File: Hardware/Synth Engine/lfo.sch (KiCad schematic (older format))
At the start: 26 parts, among them J12 Conn_01x08, J5 Conn_01x02, J6 Conn_01x03, U4 TL074, U5 TL074

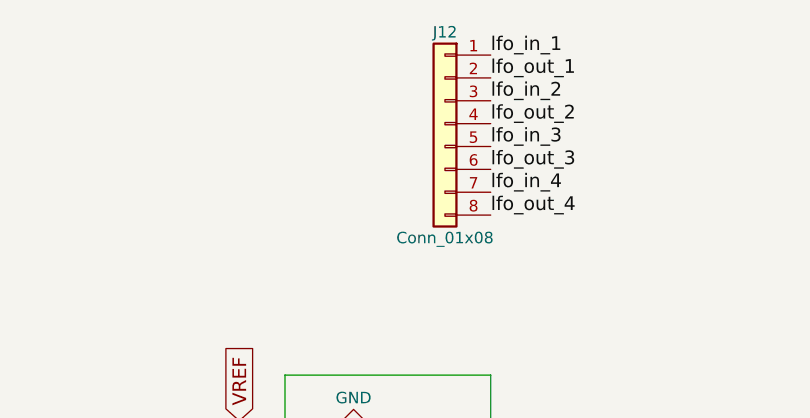
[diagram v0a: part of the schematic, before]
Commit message: fix LFO connector schem
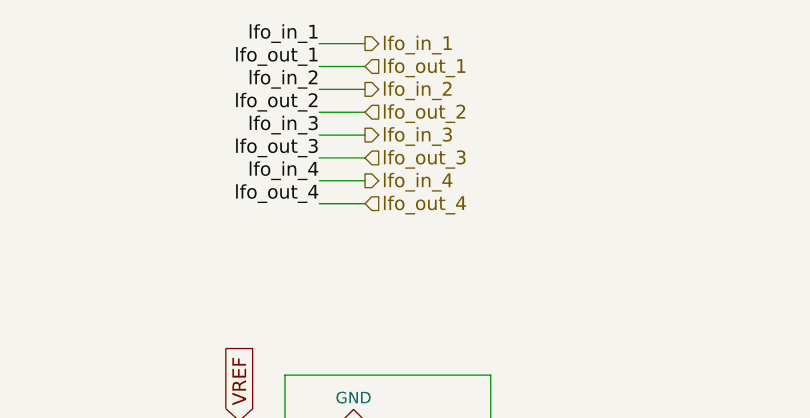
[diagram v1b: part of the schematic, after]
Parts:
- removed J12: Conn_01x08, Pin_Headers:Pin_Header_Straight_1x08_Pitch2.54mm, symbol Conn_01x08
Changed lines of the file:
@@
 Text Label 10000 5250 0    60   ~ 0
 lfo_out_4
-Text Label 6350 800  0    60   ~ 0
+Text Label 5600 750  2    60   ~ 0
 lfo_in_1
-Text Label 6350 900  0    60   ~ 0
+Text Label 5600 850  2    60   ~ 0
 lfo_out_1
-Text Label 6350 1000 0    60   ~ 0
+Text Label 5600 950  2    60   ~ 0
 lfo_in_2
-Text Label 6350 1100 0    60   ~ 0
+Text Label 5600 1050 2    60   ~ 0
 lfo_out_2
-Text Label 6350 1200 0    60   ~ 0
+Text Label 5600 1150 2    60   ~ 0
 lfo_in_3
-Text Label 6350 1300 0    60   ~ 0
+Text Label 5600 1250 2    60   ~ 0
 lfo_out_3
-Text Label 6350 1400 0    60   ~ 0
+Text Label 5600 1350 2    60   ~ 0
 lfo_in_4
-Text Label 6350 1500 0    60   ~ 0
+Text Label 5600 1450 2    60   ~ 0
 lfo_out_4
-$Comp
-L Conn_01x08 J12
-U 1 1 5C638F36
-P 6150 1100
-F 0 "J12" H 6150 1500 50  0000 C CNN
-F 1 "Conn_01x08" H 6150 600 50  0000 C CNN
-F 2 "Pin_Headers:Pin_Header_Straight_1x08_Pitch2.54mm" H 6150 1100 50  0001 C CNN
-F 3 "" H 6150 1100 50  0001 C CNN
-	1    6150 1100
-	-1   0    0    -1
-$EndComp
+Text HLabel 5800 750  2    60   Output ~ 0
+lfo_in_1
+Text HLabel 5800 850  2    60   Input ~ 0
+lfo_out_1
+Text HLabel 5800 950  2    60   Output ~ 0
+lfo_in_2
+Text HLabel 5800 1050 2    60   Input ~ 0
+lfo_out_2
+Text HLabel 5800 1150 2    60   Output ~ 0
+lfo_in_3
+Text HLabel 5800 1250 2    60   Input ~ 0
+lfo_out_3
+Text HLabel 5800 1350 2    60   Output ~ 0
+lfo_in_4
+Text HLabel 5800 1450 2    60   Input ~ 0
+lfo_out_4
+Wire Wire Line
+	5600 750  5800 750
+Wire Wire Line
+	5600 850  5800 850
+Wire Wire Line
+	5800 950  5600 950
+Wire Wire Line
+	5600 1050 5800 1050
+Wire Wire Line
+	5800 1150 5600 1150
+Wire Wire Line
+	5600 1250 5800 1250
+Wire Wire Line
+	5800 1350 5600 1350
+Wire Wire Line
+	5600 1450 5800 1450
 $EndSCHEMATC

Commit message: route LFO
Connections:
- net main_lfo: now also U5.10 (+), U5.12 (+), U5.5 (+); no longer U5.10 (+), U5.12 (+), U5.5 (+)
- new net: C76.1, U5.13 (-), U5.14
- new net: C74.1, U5.8, U5.9 (-)
- new net: C77.1, U5.6 (-), U5.7
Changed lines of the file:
@@
 $Comp
 L TL074 U5
-U 2 1 5C542164
+U 4 1 5C542164
 P 9250 2750
 F 0 "U5" H 9250 2950 50  0000 L CNN
@@
 F 2 "digikey-footprints:SOIC-14_W3.9mm" H 9200 2850 50  0001 C CNN
 F 3 "" H 9300 2950 50  0001 C CNN
-	2    9250 2750
+	4    9250 2750
 	1    0    0    1
 $EndComp
@@
 $Comp
 L TL074 U5
-U 4 1 5C5423F2
+U 3 1 5C5423F2
 P 5800 4950
 F 0 "U5" H 5800 5150 50  0000 L CNN
@@
 F 2 "digikey-footprints:SOIC-14_W3.9mm" H 5750 5050 50  0001 C CNN
 F 3 "" H 5850 5150 50  0001 C CNN
-	4    5800 4950
+	3    5800 4950
 	1    0    0    1
 $EndComp
@@
 $Comp
 L TL074 U5
-U 3 1 5C5426EC
+U 2 1 5C5426EC
 P 9300 4950
 F 0 "U5" H 9300 5150 50  0000 L CNN
@@
 F 2 "digikey-footprints:SOIC-14_W3.9mm" H 9250 5050 50  0001 C CNN
 F 3 "" H 9350 5150 50  0001 C CNN
-	3    9300 4950
+	2    9300 4950
 	1    0    0    1
 $EndComp

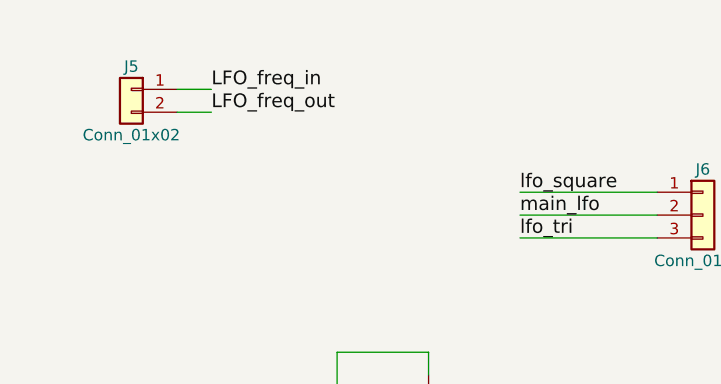
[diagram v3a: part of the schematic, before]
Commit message: fix remaining connector placement. Routing still WIP
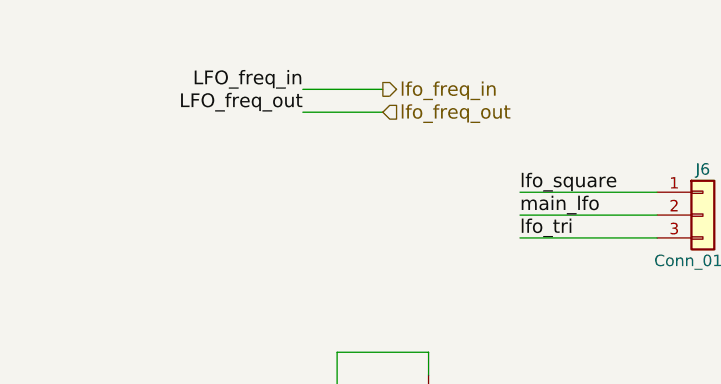
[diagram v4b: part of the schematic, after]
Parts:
- removed J5: Conn_01x02, Pin_Headers:Pin_Header_Straight_1x02_Pitch2.54mm, symbol Conn_01x02
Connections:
- net LFO_freq_in renamed lfo_freq_in
- net LFO_freq_out renamed lfo_freq_out
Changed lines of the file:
@@
 $Descr A4 11693 8268
 encoding utf-8
-Sheet 6 8
+Sheet 8 8
 Title ""
 Date ""
@@
 lfo4
 $Comp
-L GND #PWR085
+L GND #PWR0126
 U 1 1 5C37F537
 P 1450 3300
-F 0 "#PWR085" H 1450 3050 50  0001 C CNN
+F 0 "#PWR0126" H 1450 3050 50  0001 C CNN
 F 1 "GND" H 1450 3150 50  0000 C CNN
 F 2 "" H 1450 3300 50  0001 C CNN
@@
 $EndComp
 $Comp
-L GND #PWR086
+L GND #PWR0127
 U 1 1 5C37F5BA
 P 3050 3400
-F 0 "#PWR086" H 3050 3150 50  0001 C CNN
+F 0 "#PWR0127" H 3050 3150 50  0001 C CNN
 F 1 "GND" H 3050 3250 50  0000 C CNN
 F 2 "" H 3050 3400 50  0001 C CNN
@@
 $EndComp
 $Comp
-L +15V #PWR087
+L +15V #PWR0128
 U 1 1 5C37FA4D
 P 1450 3900
-F 0 "#PWR087" H 1450 3750 50  0001 C CNN
+F 0 "#PWR0128" H 1450 3750 50  0001 C CNN
 F 1 "+15V" H 1450 4040 50  0000 C CNN
 F 2 "" H 1450 3900 50  0001 C CNN
@@
 $EndComp
 $Comp
-L +15V #PWR088
+L +15V #PWR0129
 U 1 1 5C37FAD0
 P 3050 4000
-F 0 "#PWR088" H 3050 3850 50  0001 C CNN
+F 0 "#PWR0129" H 3050 3850 50  0001 C CNN
 F 1 "+15V" H 3050 4140 50  0000 C CNN
 F 2 "" H 3050 4000 50  0001 C CNN
@@
 $EndComp
 $Comp
-L GND #PWR089
+L GND #PWR0130
 U 1 1 5C381B69
 P 4050 4050
-F 0 "#PWR089" H 4050 3800 50  0001 C CNN
+F 0 "#PWR0130" H 4050 3800 50  0001 C CNN
 F 1 "GND" H 4050 3900 50  0000 C CNN
 F 2 "" H 4050 4050 50  0001 C CNN
@@
 $EndComp
 $Comp
-L GND #PWR090
+L GND #PWR0131
 U 1 1 5C38F259
 P 2300 3000
-F 0 "#PWR090" H 2300 2750 50  0001 C CNN
+F 0 "#PWR0131" H 2300 2750 50  0001 C CNN
 F 1 "GND" H 2300 2850 50  0000 C CNN
 F 2 "" H 2300 3000 50  0001 C CNN
@@
 $EndComp
 $Comp
-L GND #PWR091
+L GND #PWR0132
 U 1 1 5C50BC49
 P 2550 3000
-F 0 "#PWR091" H 2550 2750 50  0001 C CNN
+F 0 "#PWR0132" H 2550 2750 50  0001 C CNN
 F 1 "GND" H 2550 2850 50  0000 C CNN
 F 2 "" H 2550 3000 50  0001 C CNN
@@
 main_lfo
 $Comp
-L GND #PWR092
+L GND #PWR0133
 U 1 1 5C541D9A
 P 5750 2450
-F 0 "#PWR092" H 5750 2200 50  0001 C CNN
+F 0 "#PWR0133" H 5750 2200 50  0001 C CNN
 F 1 "GND" H 5750 2300 50  0000 C CNN
 F 2 "" H 5750 2450 50  0001 C CNN
@@
 $EndComp
 $Comp
-L +15V #PWR093
+L +15V #PWR0134
 U 1 1 5C541DA0
 P 5750 3050
-F 0 "#PWR093" H 5750 2900 50  0001 C CNN
+F 0 "#PWR0134" H 5750 2900 50  0001 C CNN
 F 1 "+15V" H 5750 3190 50  0000 C CNN
 F 2 "" H 5750 3050 50  0001 C CNN
@@
 main_lfo
 $Comp
-L GND #PWR094
+L GND #PWR0135
 U 1 1 5C542158
 P 9150 2450
-F 0 "#PWR094" H 9150 2200 50  0001 C CNN
+F 0 "#PWR0135" H 9150 2200 50  0001 C CNN
 F 1 "GND" H 9150 2300 50  0000 C CNN
 F 2 "" H 9150 2450 50  0001 C CNN
@@
 $EndComp
 $Comp
-L +15V #PWR095
+L +15V #PWR0136
 U 1 1 5C54215E
 P 9150 3050
-F 0 "#PWR095" H 9150 2900 50  0001 C CNN
+F 0 "#PWR0136" H 9150 2900 50  0001 C CNN
 F 1 "+15V" H 9150 3190 50  0000 C CNN
 F 2 "" H 9150 3050 50  0001 C CNN
@@
 main_lfo
 $Comp
-L GND #PWR096
+L GND #PWR0137
 U 1 1 5C5423E6
 P 5700 4650
-F 0 "#PWR096" H 5700 4400 50  0001 C CNN
+F 0 "#PWR0137" H 5700 4400 50  0001 C CNN
 F 1 "GND" H 5700 4500 50  0000 C CNN
 F 2 "" H 5700 4650 50  0001 C CNN
@@
 $EndComp
 $Comp
-L +15V #PWR097
+L +15V #PWR0138
 U 1 1 5C5423EC
 P 5700 5250
-F 0 "#PWR097" H 5700 5100 50  0001 C CNN
+F 0 "#PWR0138" H 5700 5100 50  0001 C CNN
 F 1 "+15V" H 5700 5390 50  0000 C CNN
 F 2 "" H 5700 5250 50  0001 C CNN
@@
 main_lfo
 $Comp
-L GND #PWR098
+L GND #PWR0139
 U 1 1 5C5426E0
 P 9200 4650
-F 0 "#PWR098" H 9200 4400 50  0001 C CNN
+F 0 "#PWR0139" H 9200 4400 50  0001 C CNN
 F 1 "GND" H 9200 4500 50  0000 C CNN
 F 2 "" H 9200 4650 50  0001 C CNN
@@
 $EndComp
 $Comp
-L +15V #PWR099
+L +15V #PWR0140
 U 1 1 5C5426E6
 P 9200 5250
-F 0 "#PWR099" H 9200 5100 50  0001 C CNN
+F 0 "#PWR0140" H 9200 5100 50  0001 C CNN
 F 1 "+15V" H 9200 5390 50  0000 C CNN
 F 2 "" H 9200 5250 50  0001 C CNN
@@
 Wire Wire Line
 	2700 1500 3300 1500
-$Comp
-L Conn_01x02 J5
-U 1 1 5C5E39A1
-P 1000 950
-F 0 "J5" H 1000 1050 50  0000 C CNN
-F 1 "Conn_01x02" H 1000 750 50  0000 C CNN
-F 2 "Pin_Headers:Pin_Header_Straight_1x02_Pitch2.54mm" H 1000 950 50  0001 C CNN
-F 3 "" H 1000 950 50  0001 C CNN
-	1    1000 950
-	-1   0    0    -1
-$EndComp
-Wire Wire Line
-	1200 950  1350 950
-Wire Wire Line
-	1350 1050 1200 1050
-Text Label 1350 950  0    60   ~ 0
+Wire Wire Line
+	1750 950  2100 950
+Wire Wire Line
+	1750 1050 2100 1050
+Text Label 1750 950  2    60   ~ 0
 LFO_freq_in
-Text Label 1350 1050 0    60   ~ 0
+Text Label 1750 1050 2    60   ~ 0
 LFO_freq_out
 Text Label 2300 3400 2    60   ~ 0
@@
 Wire Wire Line
 	5600 1450 5800 1450
+Text HLabel 2100 950  2    60   Output ~ 0
+lfo_freq_in
+Text HLabel 2100 1050 2    60   Input ~ 0
+lfo_freq_out
 $EndSCHEMATC
